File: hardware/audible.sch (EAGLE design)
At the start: 6 parts, among them J1 SQUALL_HEADER, J2 HIROSE-DF40C-10DP-0.4V, J3 HIROSE-DF40C-10DP-0.4V, J5 TC2030-JLINK-NL

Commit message: ripped up blees board
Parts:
- removed D1: BLUE, SparkFun-LED:LED0603
- removed R1: 1kΩ, passives:RESISTOR0402_RES
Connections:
- removed net N$2: D1.A, R1.1
- net P25: no longer D1.C
- net VCC: no longer R1.2
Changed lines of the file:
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@@
 <layers>
 <layer number="1" name="Top" color="4" fill="1" visible="no" active="no"/>
+<layer number="2" name="Route2" color="1" fill="3" visible="no" active="no"/>
+<layer number="3" name="Route3" color="4" fill="3" visible="no" active="no"/>
+<layer number="4" name="Route4" color="1" fill="4" visible="no" active="no"/>
+<layer number="5" name="Route5" color="4" fill="4" visible="no" active="no"/>
+<layer number="6" name="Route6" color="1" fill="8" visible="no" active="no"/>
+<layer number="7" name="Route7" color="4" fill="8" visible="no" active="no"/>
+<layer number="8" name="Route8" color="1" fill="2" visible="no" active="no"/>
+<layer number="9" name="Route9" color="4" fill="2" visible="no" active="no"/>
+<layer number="10" name="Route10" color="1" fill="7" visible="no" active="no"/>
+<layer number="11" name="Route11" color="4" fill="7" visible="no" active="no"/>
+<layer number="12" name="Route12" color="1" fill="5" visible="no" active="no"/>
+<layer number="13" name="Route13" color="4" fill="5" visible="no" active="no"/>
+<layer number="14" name="Route14" color="1" fill="6" visible="no" active="no"/>
+<layer number="15" name="Route15" color="4" fill="6" visible="no" active="no"/>
 <layer number="16" name="Bottom" color="1" fill="1" visible="no" active="no"/>
 <layer number="17" name="Pads" color="2" fill="1" visible="no" active="no"/>
@@
 <layer number="54" name="bGND_GNDA" color="1" fill="9" visible="no" active="no"/>
 <layer number="56" name="wert" color="7" fill="1" visible="no" active="no"/>
-<layer number="90" name="Modules" color="5" fill="1" visible="yes" active="yes"/>
 <layer number="91" name="Nets" color="2" fill="1" visible="yes" active="yes"/>
 <layer number="92" name="Busses" color="1" fill="1" visible="yes" active="yes"/>
@@
 <schematic xreflabel="%F%N/%S.%C%R" xrefpart="/%S.%C%R">
 <attributes>
+<attribute name="AUTHOR" value="BLEES Dev Team"/>
+<attribute name="REV" value="A"/>
+<attribute name="TITLE" value="BLEES Sensor Board"/>
 </attributes>
 <variantdefs>
@@
 <part name="P+4" library="supply1" deviceset="VCC" device=""/>
 <part name="GND9" library="supply1" deviceset="GND" device=""/>
-<part name="D1" library="SparkFun-LED" deviceset="LED" device="0603" value="BLUE"/>
-<part name="R1" library="passives" deviceset="RESISTOR" device="0402_RES" value="1kΩ"/>
-<part name="P+9" library="supply1" deviceset="VCC" device=""/>
 <part name="J5" library="connector" deviceset="TC2030-JLINK" device="-NL"/>
 <part name="P+7" library="supply1" deviceset="VCC" device=""/>
@@
 </parts>
 <sheets>
-<sheet>
-<plain>
-</plain>
-<instances>
-</instances>
-<busses>
-</busses>
-<nets>
-</nets>
-</sheet>
 <sheet>
 <plain>
@@
 <instance part="P+4" gate="VCC" x="81.28" y="170.18"/>
 <instance part="GND9" gate="1" x="104.14" y="142.24"/>
-<instance part="D1" gate="G$1" x="162.56" y="157.48"/>
-<instance part="R1" gate="G$1" x="162.56" y="167.64" rot="R90"/>
-<instance part="P+9" gate="VCC" x="162.56" y="177.8"/>
-<instance part="J5" gate="G$1" x="198.12" y="162.56"/>
-<instance part="P+7" gate="VCC" x="182.88" y="172.72"/>
-<instance part="GND8" gate="1" x="182.88" y="149.86"/>
+<instance part="J5" gate="G$1" x="177.8" y="157.48"/>
+<instance part="P+7" gate="VCC" x="162.56" y="167.64"/>
+<instance part="GND8" gate="1" x="162.56" y="144.78"/>
 </instances>
 <busses>
@@
 </segment>
 <segment>
-<pinref part="R1" gate="G$1" pin="2"/>
-<pinref part="P+9" gate="VCC" pin="VCC"/>
-<wire x1="162.56" y1="175.26" x2="162.56" y2="172.72" width="0.1524" layer="91"/>
-</segment>
-<segment>
 <pinref part="J5" gate="G$1" pin="VCC"/>
 <pinref part="P+7" gate="VCC" pin="VCC"/>
-<wire x1="185.42" y1="167.64" x2="182.88" y2="167.64" width="0.1524" layer="91"/>
-<wire x1="182.88" y1="167.64" x2="182.88" y2="170.18" width="0.1524" layer="91"/>
+<wire x1="165.1" y1="162.56" x2="162.56" y2="162.56" width="0.1524" layer="91"/>
+<wire x1="162.56" y1="162.56" x2="162.56" y2="165.1" width="0.1524" layer="91"/>
 </segment>
 </net>
@@
 <segment>
 <pinref part="GND8" gate="1" pin="GND"/>
-<wire x1="182.88" y1="152.4" x2="182.88" y2="157.48" width="0.1524" layer="91"/>
+<wire x1="162.56" y1="147.32" x2="162.56" y2="152.4" width="0.1524" layer="91"/>
 <pinref part="J5" gate="G$1" pin="GND"/>
-<wire x1="182.88" y1="157.48" x2="185.42" y2="157.48" width="0.1524" layer="91"/>
+<wire x1="162.56" y1="152.4" x2="165.1" y2="152.4" width="0.1524" layer="91"/>
 </segment>
 </net>
@@
 <label x="104.14" y="154.94" size="1.27" layer="95" xref="yes"/>
 </segment>
-<segment>
-<pinref part="D1" gate="G$1" pin="C"/>
-<wire x1="162.56" y1="149.86" x2="162.56" y2="152.4" width="0.1524" layer="91"/>
-<label x="162.56" y="149.86" size="1.778" layer="95" rot="R270" xref="yes"/>
-</segment>
 </net>
 <net name="A7" class="0">
@@
 <segment>
 <pinref part="J5" gate="G$1" pin="SWDCLK"/>
-<wire x1="213.36" y1="165.1" x2="210.82" y2="165.1" width="0.1524" layer="91"/>
-<label x="213.36" y="165.1" size="1.27" layer="95" xref="yes"/>
+<wire x1="193.04" y1="160.02" x2="190.5" y2="160.02" width="0.1524" layer="91"/>
+<label x="193.04" y="160.02" size="1.27" layer="95" xref="yes"/>
 </segment>
 </net>
@@
 <segment>
 <pinref part="J5" gate="G$1" pin="SWDIO"/>
-<wire x1="210.82" y1="167.64" x2="213.36" y2="167.64" width="0.1524" layer="91"/>
-<label x="213.36" y="167.64" size="1.27" layer="95" xref="yes"/>
+<wire x1="190.5" y1="162.56" x2="193.04" y2="162.56" width="0.1524" layer="91"/>
+<label x="193.04" y="162.56" size="1.27" layer="95" xref="yes"/>
 </segment>
 </net>
@@
 </segment>
 </net>
-<net name="N$2" class="0">
-<segment>
-<pinref part="D1" gate="G$1" pin="A"/>
-<pinref part="R1" gate="G$1" pin="1"/>
-<wire x1="162.56" y1="162.56" x2="162.56" y2="160.02" width="0.1524" layer="91"/>
-</segment>
-</net>

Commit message: Almost completed schematic
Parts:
- added C1, C2, C3: 1uF, passives:CAPACITOR
- added C4: 100n, passives:CAPACITOR
- added C5: 1u, passives:CAPACITOR
- added C6: 22uF, passives:CAPACITOR
- added IC1: LTC1966CMS8, chips:LTC1966CMS8
- added R1, R4: 14k, passives:RESISTOR0402_RES
- added R2, R5: 1k, passives:RESISTOR0402_RES
- added R3: 47k, passives:RESISTOR0402_RES
- added R6: 20k, passives:RESISTOR0402_RES
- added R7, R8, R9: 10k, passives:RESISTOR0402_RES
- added U$2: ICS-40310, chips:ICS-40310
- added U$3: LD39015, chips:LD39015
- added U1, U2: MAX417ESA+, chips:MAX417ESA+
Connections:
- new net MIC: C3.1, U$2.OUT
- new net MIC_AMP_1: R1.2, U1.INB+, U1.OUTA
- new net MIC_AMP_2: C4.1, R4.1, U1.OUTB
- new net N$1: C3.2, R3.2, U1.INA+
- new net N$10: C6.2, R6.2, R7.1, U2.INB+
- new net N$2: C4.2, IC1.IN1
- new net N$4: R1.1, R2.2, U1.INA-
- new net N$5: R4.2, R5.1, U1.INB-
- new net N$6: R8.1, U2.INB-
- new net RMS: C5.2, IC1.VOUT, U2.INA+
- new net RMS_BUF: R6.1, U2.INA-, U2.OUTA
- new net VREF: C1.1, IC1.IN2, R2.1, R3.1, R5.2, U$2.VDD, U$3.OUT
- net A7: now also R7.2, R9.1, U2.OUTB
- net GND: now also C1.2, C2.2, C5.1, C6.1, IC1.GND, IC1.RTN, IC1.VSS, R8.2, R9.2, U$2.GND, U$3.GND, U1.V-, U2.V-
- net P23: now also IC1./EN
- net VCC: now also C2.1, IC1.VDD, U$3.IN, U1.V+, U2.V+
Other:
- moved on the sheet: J3, J5

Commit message: better layout
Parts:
- added C7: 0.01uF, passives:CAPACITOR
- added C8: 0.1uF, passives:CAPACITOR
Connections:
- net GND: now also C7.1, C8.2
- net VCC: now also C7.2
- net VREF: now also C8.1
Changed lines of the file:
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@@
 <part name="C6" library="passives" deviceset="CAPACITOR" device="" value="22uF"/>
 <part name="GND12" library="umich" deviceset="GND" device=""/>
+<part name="C7" library="passives" deviceset="CAPACITOR" device="" value="0.01uF"/>
+<part name="GND13" library="umich" deviceset="GND" device=""/>
+<part name="C8" library="passives" deviceset="CAPACITOR" device="" value="0.1uF"/>
+<part name="GND14" library="umich" deviceset="GND" device=""/>
 </parts>
 <sheets>
@@
 <instance part="GND7" gate="1" x="50.8" y="48.26"/>
 <instance part="GND10" gate="1" x="132.08" y="66.04"/>
-<instance part="P+3" gate="VCC" x="48.26" y="81.28"/>
+<instance part="P+3" gate="VCC" x="48.26" y="91.44"/>
 <instance part="P+5" gate="VCC" x="165.1" y="119.38"/>
 <instance part="P+6" gate="VCC" x="193.04" y="86.36"/>
@@
 <instance part="C6" gate="G$1" x="198.12" y="53.34" rot="R180"/>
 <instance part="GND12" gate="1" x="198.12" y="45.72"/>
+<instance part="C7" gate="G$1" x="53.34" y="83.82" rot="R270"/>
+<instance part="GND13" gate="1" x="58.42" y="78.74"/>
+<instance part="C8" gate="G$1" x="20.32" y="104.14"/>
+<instance part="GND14" gate="1" x="20.32" y="93.98"/>
 </instances>
 <busses>
@@
 <pinref part="IC1" gate="G$1" pin="VDD"/>
 <pinref part="P+3" gate="VCC" pin="VCC"/>
-<wire x1="48.26" y1="76.2" x2="48.26" y2="78.74" width="0.1524" layer="91"/>
+<wire x1="48.26" y1="76.2" x2="48.26" y2="83.82" width="0.1524" layer="91"/>
+<pinref part="C7" gate="G$1" pin="2"/>
+<wire x1="48.26" y1="83.82" x2="48.26" y2="88.9" width="0.1524" layer="91"/>
+<junction x="48.26" y="83.82"/>
 </segment>
 <segment>
@@
 <wire x1="198.12" y1="48.26" x2="198.12" y2="50.8" width="0.1524" layer="91"/>
 </segment>
+<segment>
+<pinref part="C7" gate="G$1" pin="1"/>
+<wire x1="55.88" y1="83.82" x2="58.42" y2="83.82" width="0.1524" layer="91"/>
+<pinref part="GND13" gate="1" pin="GND"/>
+<wire x1="58.42" y1="83.82" x2="58.42" y2="81.28" width="0.1524" layer="91"/>
+</segment>
+<segment>
+<pinref part="C8" gate="G$1" pin="2"/>
+<pinref part="GND14" gate="1" pin="GND"/>
+<wire x1="20.32" y1="96.52" x2="20.32" y2="99.06" width="0.1524" layer="91"/>
+</segment>
 </net>
 <net name="A6" class="0">
@@
 <segment>
 <pinref part="U$2" gate="G$1" pin="VDD"/>
-<wire x1="30.48" y1="109.22" x2="27.94" y2="109.22" width="0.1524" layer="91"/>
-<label x="27.94" y="109.22" size="1.016" layer="95" rot="R180" xref="yes"/>
+<wire x1="30.48" y1="109.22" x2="20.32" y2="109.22" width="0.1524" layer="91"/>
+<label x="17.78" y="109.22" size="1.016" layer="95" rot="R180" xref="yes"/>
+<pinref part="C8" gate="G$1" pin="1"/>
+<wire x1="20.32" y1="109.22" x2="17.78" y2="109.22" width="0.1524" layer="91"/>
+<wire x1="20.32" y1="106.68" x2="20.32" y2="109.22" width="0.1524" layer="91"/>
+<junction x="20.32" y="109.22"/>
 </segment>
 <segment>
@@
 <pinref part="U2" gate="A" pin="INA-"/>
 <wire x1="129.54" y1="76.2" x2="132.08" y2="76.2" width="0.1524" layer="91"/>
-</segment>
-<segment>
+<label x="129.54" y="78.74" size="1.016" layer="95" rot="R180" xref="yes"/>
+</segment>
+<segment>

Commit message: better schematic
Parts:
- added Q1: FK3503010L, chips:FK3503010L
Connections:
- net GND: now also Q1.S
- net N$10: now also Q1.D
- net P22: now also U$3.EN
- net P24: now also Q1.G
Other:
- note added: "Buffer and Integrator"
- note added: "Jlink"
- note added: "LDO"
- note added: "Microphone"
- note added: "Microphone Preamp"
- note added: "RMS to DC"
- moved on the sheet: C3, C4, C5, C6, C7, C8, IC1, J2, J3, J5, R1, R2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

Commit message: Updated sch and brd
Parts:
- added C10, C9: 0.1uF, passives:CAPACITOR
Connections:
- net RMS renamed N$3
- net GND: now also C10.1, C9.1
- net VCC: now also C10.2, C9.2
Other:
- moved on the sheet: C3, C4, C5, C6, C7, C8, IC1, Q1, R1, R2, R3, R4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

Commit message: almost routed
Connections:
- net A5: no longer J3.9
- net A6: no longer J3.7
- net MISO: no longer J3.8
- net MOSI: no longer J3.6
- net P25: no longer J2.8
- net SCL: no longer J3.3
- net SCLK: no longer J3.10
- net SDA: no longer J3.1
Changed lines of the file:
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@@
 <?xml version="1.0" encoding="utf-8"?>
 <!DOCTYPE eagle SYSTEM "eagle.dtd">
-<eagle version="7.5.0">
+<eagle version="7.6.0">
 <drawing>
 <settings>
@@
 <label x="58.42" y="144.78" size="1.27" layer="95" xref="yes"/>
 </segment>
-<segment>
-<pinref part="J3" gate="G$1" pin="7"/>
-<wire x1="116.84" y1="154.94" x2="111.76" y2="154.94" width="0.1524" layer="91"/>
-<label x="111.76" y="154.94" size="1.27" layer="95" rot="R180" xref="yes"/>
-</segment>
 </net>
 <net name="SCLK" class="0">
@@
 <label x="58.42" y="160.02" size="1.27" layer="95" xref="yes"/>
 </segment>
-<segment>
-<pinref part="J3" gate="G$1" pin="10"/>
-<wire x1="124.46" y1="152.4" x2="129.54" y2="152.4" width="0.1524" layer="91"/>
-<label x="129.54" y="152.4" size="1.27" layer="95" xref="yes"/>
-</segment>
 </net>
 <net name="MOSI" class="0">
@@
 <label x="58.42" y="165.1" size="1.27" layer="95" xref="yes"/>
 </segment>
-<segment>
-<pinref part="J3" gate="G$1" pin="6"/>
-<wire x1="124.46" y1="157.48" x2="129.54" y2="157.48" width="0.1524" layer="91"/>
-<label x="129.54" y="157.48" size="1.27" layer="95" xref="yes"/>
-</segment>
 </net>
 <net name="MISO" class="0">
@@
 <label x="58.42" y="162.56" size="1.27" layer="95" xref="yes"/>
 </segment>
-<segment>
-<pinref part="J3" gate="G$1" pin="8"/>
-<wire x1="124.46" y1="154.94" x2="129.54" y2="154.94" width="0.1524" layer="91"/>
-<label x="129.54" y="154.94" size="1.27" layer="95" xref="yes"/>
-</segment>
 </net>
 <net name="A5" class="0">
@@
 <label x="58.42" y="147.32" size="1.27" layer="95" xref="yes"/>
 </segment>
-<segment>
-<pinref part="J3" gate="G$1" pin="9"/>
-<wire x1="111.76" y1="152.4" x2="116.84" y2="152.4" width="0.1524" layer="91"/>
-<label x="111.76" y="152.4" size="1.27" layer="95" rot="R180" xref="yes"/>
-</segment>
 </net>
 <net name="P23" class="0">
@@
 <label x="58.42" y="154.94" size="1.27" layer="95" xref="yes"/>
 </segment>
-<segment>
-<pinref part="J3" gate="G$1" pin="1"/>
-<wire x1="116.84" y1="162.56" x2="111.76" y2="162.56" width="0.1524" layer="91"/>
-<label x="111.76" y="162.56" size="1.27" layer="95" rot="R180" xref="yes"/>
-</segment>
 </net>
 <net name="SCL" class="0">
@@
 <label x="58.42" y="152.4" size="1.27" layer="95" xref="yes"/>
 </segment>
-<segment>
-<pinref part="J3" gate="G$1" pin="3"/>
-<wire x1="116.84" y1="160.02" x2="111.76" y2="160.02" width="0.1524" layer="91"/>
-<label x="111.76" y="160.02" size="1.27" layer="95" rot="R180" xref="yes"/>
-</segment>
 </net>
 <net name="P25" class="0">
@@
 <label x="58.42" y="129.54" size="1.27" layer="95" xref="yes"/>
 </segment>
-<segment>
-<pinref part="J2" gate="G$1" pin="8"/>
-<wire x1="88.9" y1="154.94" x2="96.52" y2="154.94" width="0.1524" layer="91"/>
-<label x="96.52" y="154.94" size="1.27" layer="95" xref="yes"/>
-</segment>
-</net>
+</net>

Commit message: routed
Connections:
- removed net A5: J1.A5
- removed net A6: J1.A6
- removed net MISO: J1.MISO
- removed net MOSI: J1.MOSI
- removed net P25: J1.P25
- removed net SCL: J1.SCL
- removed net SCLK: J1.SCLK
- removed net SDA: J1.SDA
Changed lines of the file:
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@@
-</segment>
-</net>
-<net name="A6" class="0">
-<segment>
-<pinref part="J1" gate="G$1" pin="A6"/>
-<wire x1="55.88" y1="144.78" x2="58.42" y2="144.78" width="0.1524" layer="91"/>
-<label x="58.42" y="144.78" size="1.27" layer="95" xref="yes"/>
-</segment>
-</net>
-<net name="SCLK" class="0">
-<segment>
-<pinref part="J1" gate="G$1" pin="SCLK"/>
-<wire x1="55.88" y1="160.02" x2="58.42" y2="160.02" width="0.1524" layer="91"/>
-<label x="58.42" y="160.02" size="1.27" layer="95" xref="yes"/>
-</segment>
-</net>
-<net name="MOSI" class="0">
-<segment>
-<pinref part="J1" gate="G$1" pin="MOSI"/>
-<wire x1="55.88" y1="165.1" x2="58.42" y2="165.1" width="0.1524" layer="91"/>
-<label x="58.42" y="165.1" size="1.27" layer="95" xref="yes"/>
-</segment>
-</net>
-<net name="MISO" class="0">
-<segment>
-<pinref part="J1" gate="G$1" pin="MISO"/>
-<wire x1="55.88" y1="162.56" x2="58.42" y2="162.56" width="0.1524" layer="91"/>
-<label x="58.42" y="162.56" size="1.27" layer="95" xref="yes"/>
-</segment>
-</net>
-<net name="A5" class="0">
-<segment>
-<pinref part="J1" gate="G$1" pin="A5"/>
-<wire x1="55.88" y1="147.32" x2="58.42" y2="147.32" width="0.1524" layer="91"/>
-<label x="58.42" y="147.32" size="1.27" layer="95" xref="yes"/>
 </segment>
 </net>
@@
 </segment>
 </net>
-<net name="SDA" class="0">
-<segment>
-<pinref part="J1" gate="G$1" pin="SDA"/>
-<wire x1="55.88" y1="154.94" x2="58.42" y2="154.94" width="0.1524" layer="91"/>
-<label x="58.42" y="154.94" size="1.27" layer="95" xref="yes"/>
-</segment>
-</net>
-<net name="SCL" class="0">
-<segment>
-<pinref part="J1" gate="G$1" pin="SCL"/>
-<wire x1="55.88" y1="152.4" x2="58.42" y2="152.4" width="0.1524" layer="91"/>
-<label x="58.42" y="152.4" size="1.27" layer="95" xref="yes"/>
-</segment>
-</net>
-<net name="P25" class="0">
-<segment>
-<pinref part="J1" gate="G$1" pin="P25"/>
-<wire x1="55.88" y1="129.54" x2="58.42" y2="129.54" width="0.1524" layer="91"/>
-<label x="58.42" y="129.54" size="1.27" layer="95" xref="yes"/>
-</segment>
-</net>

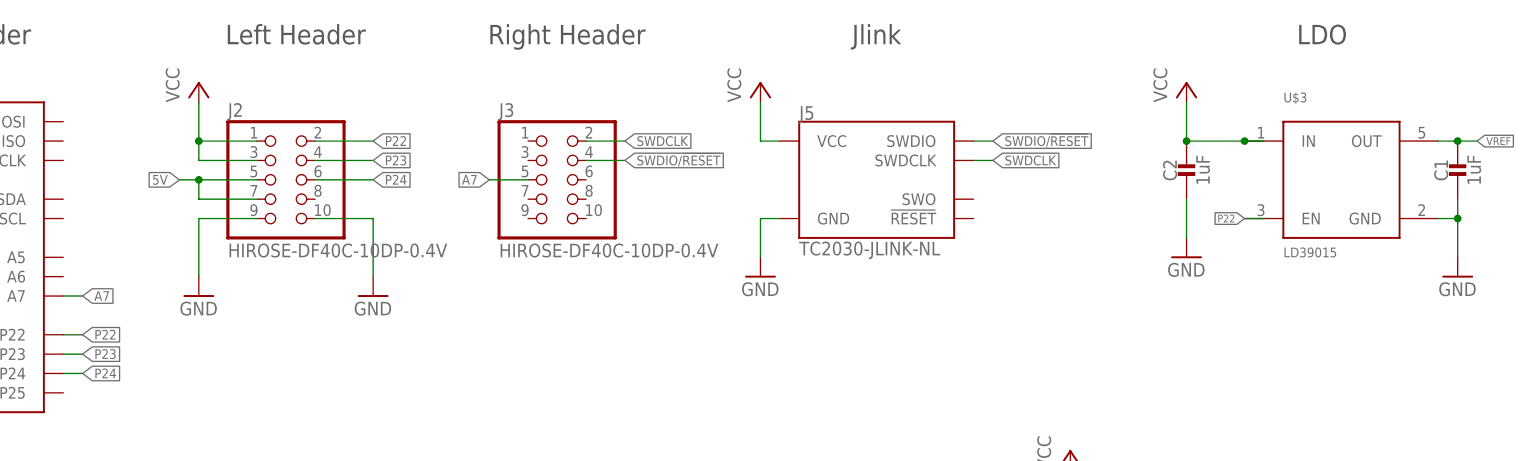
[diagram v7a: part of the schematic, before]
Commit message: Removed headers and fixed wire angles
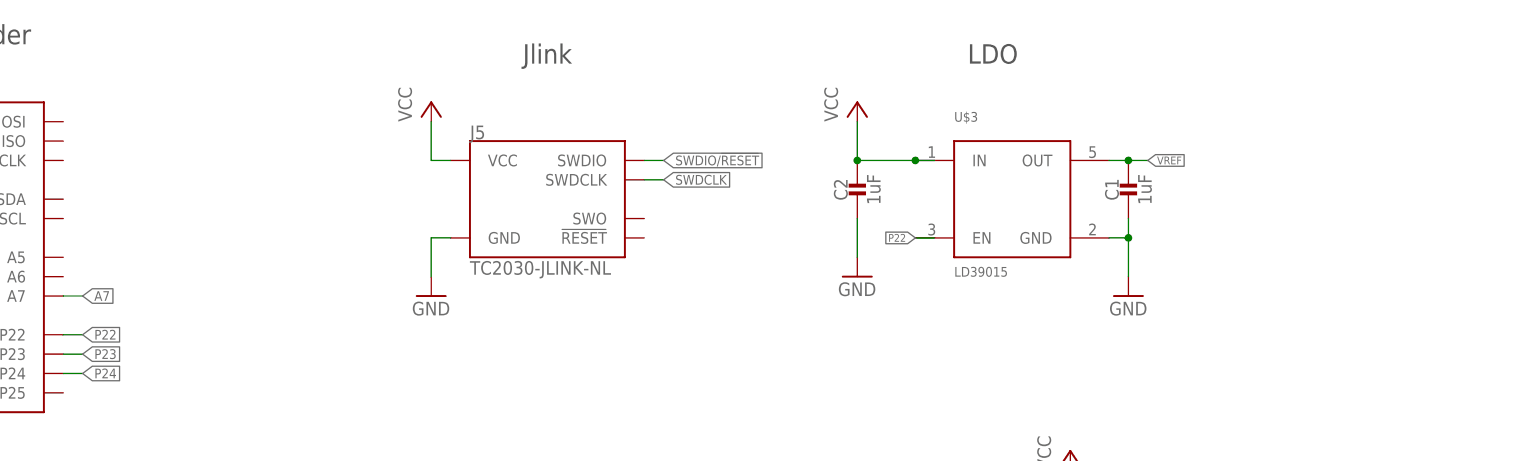
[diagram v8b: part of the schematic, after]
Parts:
- removed J2, J3: HIROSE-DF40C-10DP-0.4V, headers:HIROSE-DF40C-10DP-0.4V
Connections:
- net 5V: no longer J2.5, J2.7
- net A7: no longer J3.5
- net GND: no longer J2.10, J2.9
- net P22: no longer J2.2
- net P23: no longer J2.4
- net P24: no longer J2.6
- net SWDCLK: no longer J3.2
- net SWDIO/!RESET: no longer J3.4
- net VCC: no longer J2.1, J2.3
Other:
- note removed: "Left Header"
- note removed: "Right Header"
- moved on the sheet: C1, C2, J5, U$3
